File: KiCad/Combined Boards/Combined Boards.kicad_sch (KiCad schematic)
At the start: 0 parts

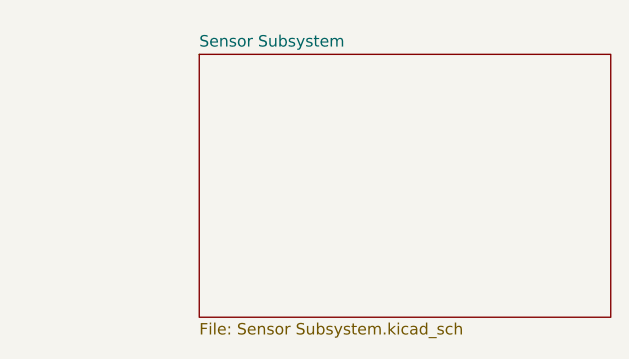
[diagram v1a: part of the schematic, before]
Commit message: Updated combined board schematics
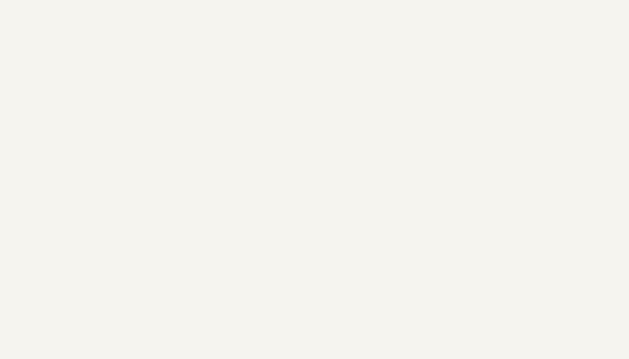
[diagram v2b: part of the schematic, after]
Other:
- removed sheet Sensor Subsystem
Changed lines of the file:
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@@
   (title_block
     (title "Combined Wireless Sensor Boards Master Sheet")
-    (date "2023-08-01")
+    (date "2023-09-19")
     (rev "A.1")
     (company "NSE Labs")
   )
-  (sheet (at 195.58 72.39) (size 45.72 29.21) (fields_autoplaced)
-    (stroke (width 0.1524) (type solid))
-    (fill (color 0 0 0 0.0000))
-    (property "Sheetname" "Sensor Subsystem" (at 195.58 71.6784 0) (show_name)
-      (effects (font (size 1.27 1.27)) (justify left bottom))
-    )
-    (property "Sheetfile" "Sensor Subsystem.kicad_sch" (at 195.58 102.1846 0)
-      (effects (font (size 1.27 1.27)) (justify left top))
-    )
-    (instances
-      (project "Combined Boards"
-        (path "/819f9f2e-5083-42df-b63a-6cdcb84600f5" (page "4"))
-      )
-    )
-  )
   (sheet (at 119.38 72.39) (size 48.26 29.21) (fields_autoplaced)
